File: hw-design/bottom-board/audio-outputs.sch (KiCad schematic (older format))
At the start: 54 parts, among them J10 NMJ6HCD2, J9 NMJ6HCD2, K1 G6S-2, K2 G6S-2, Q1 2N7002, Q2 2N7002, U11 OPA1678, U12 OPA1678

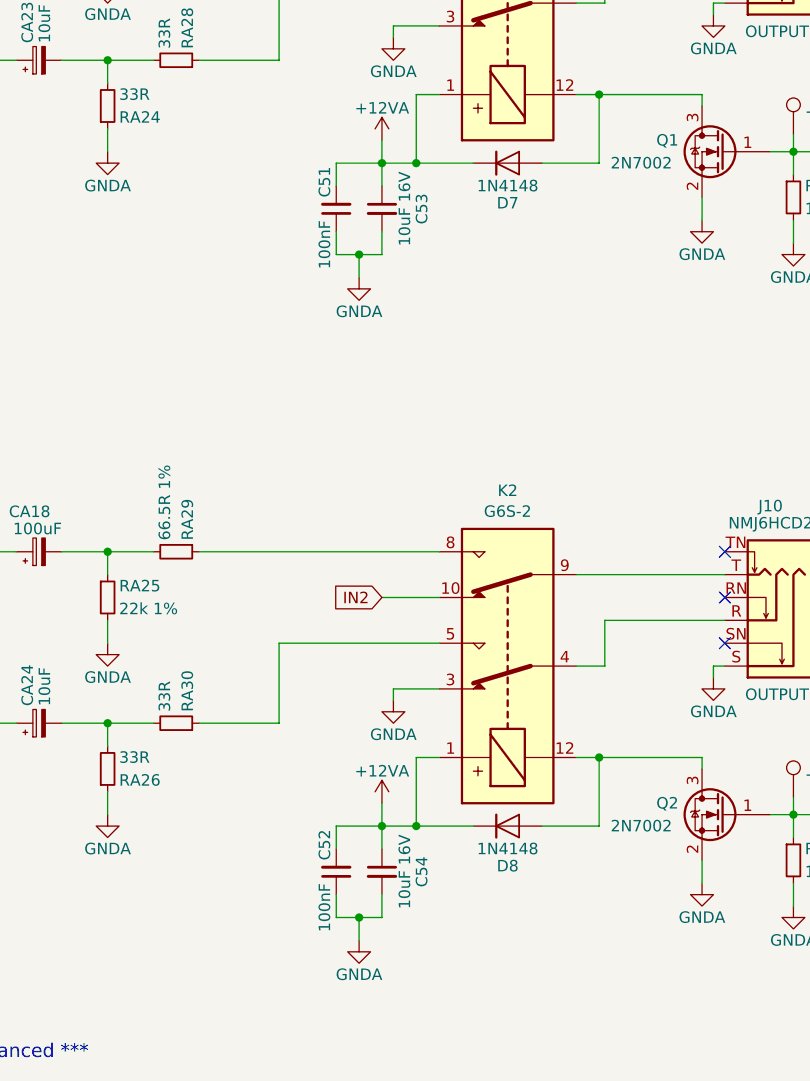
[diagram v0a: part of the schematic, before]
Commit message: increase filtering caps next to delay, less noise on low freqs
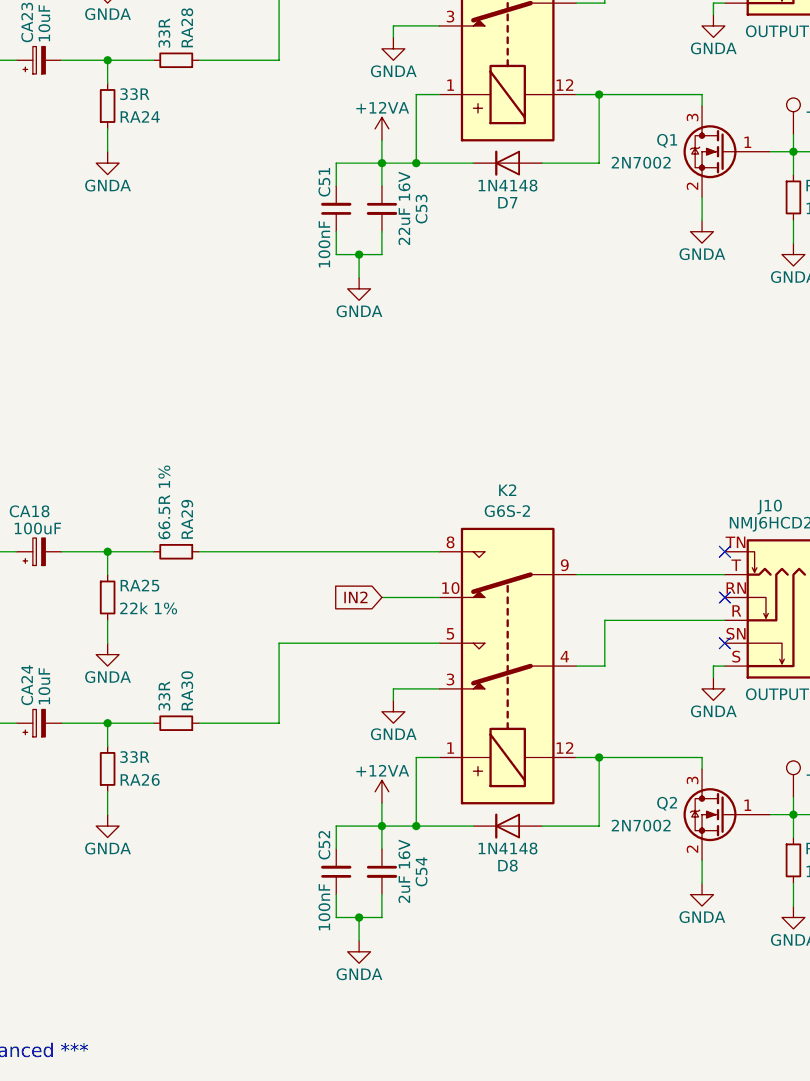
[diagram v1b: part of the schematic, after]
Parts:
- C53: value 10uF 16V -> 22uF 16V; MPN CL21A106KOFNNNE -> GRM21BC81C226ME44L; MPN2 C2012X5R1C106M085AC -> (none)
- C54: value 10uF 16V -> 2uF 16V; MPN CL21A106KOFNNNE -> GRM21BC81C226ME44L; MPN2 C2012X5R1C106M085AC -> (none)
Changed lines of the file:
@@
 AR Path="/54F72CD0/5BE997ED" Ref="C53"  Part="1"
 F 0 "C53" V 6625 3150 50  0000 C CNN
-F 1 "10uF 16V" V 6700 3150 50  0000 C CNN
+F 1 "22uF 16V" V 6700 3150 50  0000 C CNN
 F 2 "Capacitor_SMD:C_0805_2012Metric" H 6800 3150 60  0001 C CNN
 F 3 "" H 6800 3150 60  0000 C CNN
-F 4 "CL21A106KOFNNNE" H 1500 -2200 50  0001 C CNN "MPN"
-F 5 "C2012X5R1C106M085AC" H 6800 3150 50  0001 C CNN "MPN2"
+F 4 "GRM21BC81C226ME44L" H 1500 -2200 50  0001 C CNN "MPN"
 	1    6800 3150
 	-1   0    0    -1
@@
 AR Path="/54F72CD0/5BE9AFFC" Ref="C54"  Part="1"
 F 0 "C54" V 6625 6050 50  0000 C CNN
-F 1 "10uF 16V" V 6700 6050 50  0000 C CNN
+F 1 "2uF 16V" V 6700 6050 50  0000 C CNN
 F 2 "Capacitor_SMD:C_0805_2012Metric" H 6800 6050 60  0001 C CNN
 F 3 "" H 6800 6050 60  0000 C CNN
-F 4 "CL21A106KOFNNNE" H 1500 700 50  0001 C CNN "MPN"
-F 5 "C2012X5R1C106M085AC" H 6800 6050 50  0001 C CNN "MPN2"
+F 4 "GRM21BC81C226ME44L" H 1500 700 50  0001 C CNN "MPN"
 	1    6800 6050
 	-1   0    0    -1

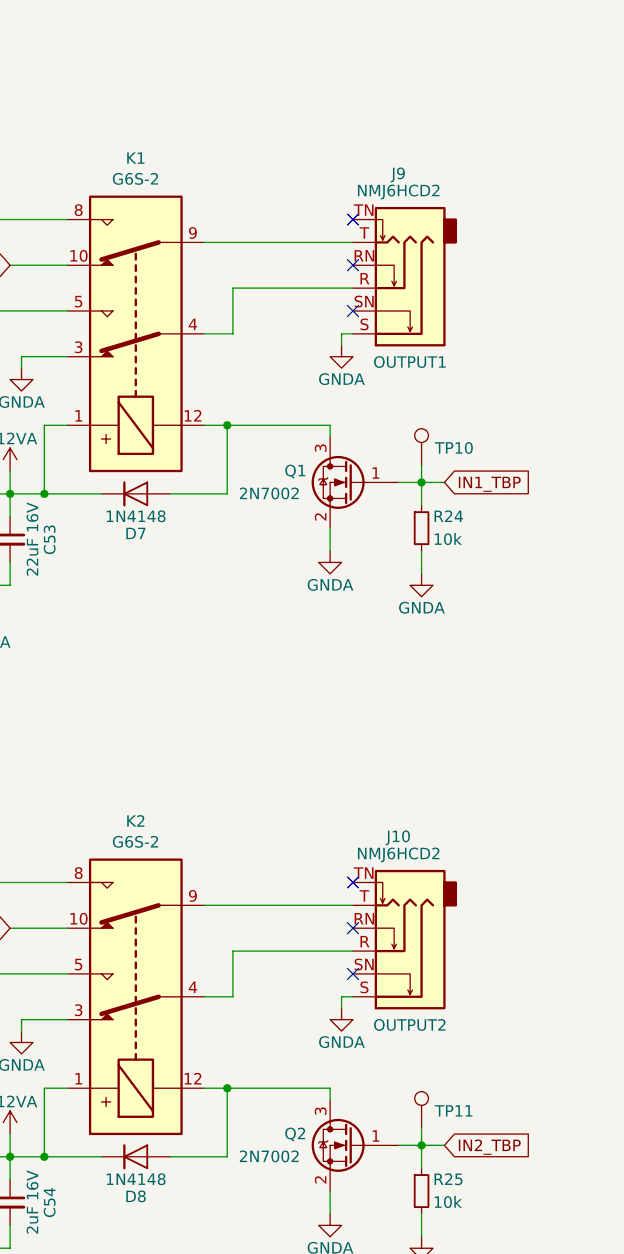
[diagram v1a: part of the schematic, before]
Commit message: added holes for new adapter + add jack detection
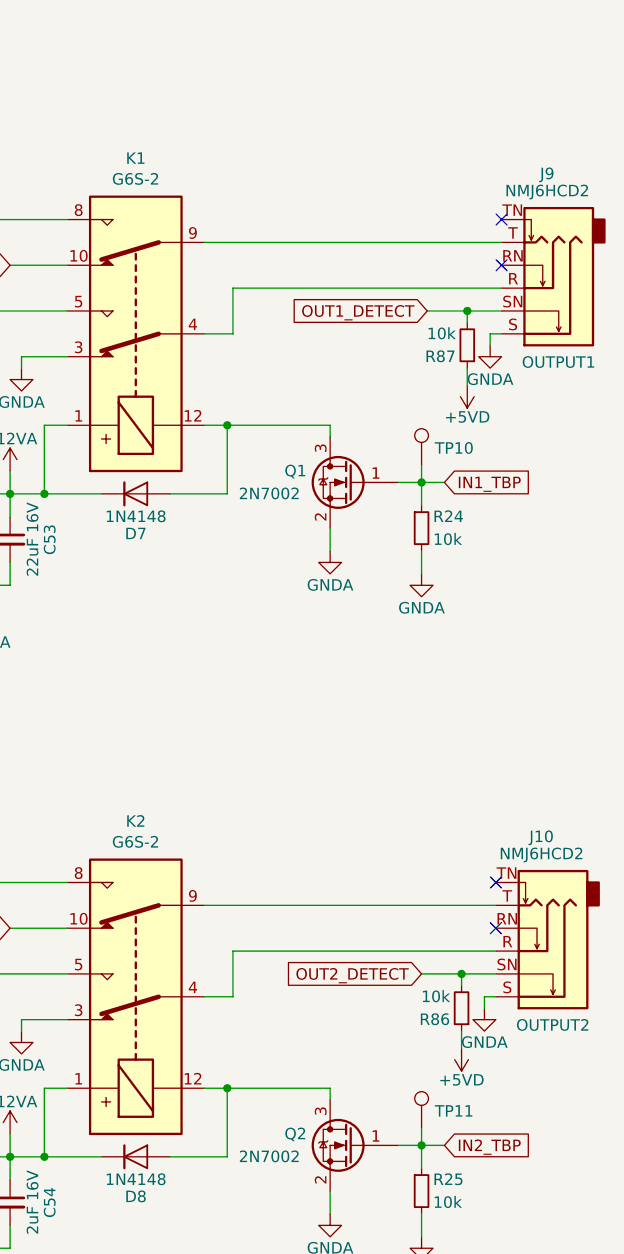
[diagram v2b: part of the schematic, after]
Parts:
- added R86, R87: 10k, Resistor_SMD:R_0603_1608Metric, symbol bottom-board-rescue:R_Small-Device
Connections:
- net OUT1_DETECT: now reaches J9.SN
- net OUT1_DETECT: now also R87.2
- net OUT2_DETECT: now reaches J10.SN
- net OUT2_DETECT: now also R86.2
- new net +5VD: R86.1, R87.1
- no-connect marks 6 -> 4
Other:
- moved on the sheet: J10, J9
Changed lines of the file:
@@
 L bottom-board-rescue:AudioJack3_Switch-Connector J9
 U 1 1 5B54B112
-P 8500 2050
-F 0 "J9" H 8500 1550 50  0000 C CNN
-F 1 "NMJ6HCD2" H 8500 1625 50  0000 C CNN
-F 2 "footprints:NMJ6HCD2" H 8750 2150 50  0001 C CNN
-F 3 "" H 8750 2150 50  0001 C CNN
-F 4 "NMJ6HCD2" H 8500 2050 60  0001 C CNN "MPN"
-F 5 "OUTPUT1" H 8450 2375 50  0000 C CNN "Comment"
-	1    8500 2050
+P 9150 2050
+F 0 "J9" H 9150 1550 50  0000 C CNN
+F 1 "NMJ6HCD2" H 9150 1625 50  0000 C CNN
+F 2 "footprints:NMJ6HCD2" H 9400 2150 50  0001 C CNN
+F 3 "" H 9400 2150 50  0001 C CNN
+F 4 "NMJ6HCD2" H 9150 2050 60  0001 C CNN "MPN"
+F 5 "OUTPUT1" H 9100 2375 50  0000 C CNN "Comment"
+	1    9150 2050
 	-1   0    0    1
 $EndComp
@@
 L bottom-board-rescue:GNDA-power #PWR0135
 U 1 1 5B54B119
-P 8250 2300
-F 0 "#PWR0135" H 8250 2050 50  0001 C CNN
-F 1 "GNDA" H 8250 2150 50  0000 C CNN
-F 2 "" H 8250 2300 60  0000 C CNN
-F 3 "" H 8250 2300 60  0000 C CNN
-	1    8250 2300
-	1    0    0    -1
-$EndComp
-NoConn ~ 8300 2150
-NoConn ~ 8300 1950
-NoConn ~ 8300 1750
+P 8900 2300
+F 0 "#PWR0135" H 8900 2050 50  0001 C CNN
+F 1 "GNDA" H 8900 2150 50  0000 C CNN
+F 2 "" H 8900 2300 60  0000 C CNN
+F 3 "" H 8900 2300 60  0000 C CNN
+	1    8900 2300
+	1    0    0    -1
+$EndComp
+NoConn ~ 8950 1950
+NoConn ~ 8950 1750
 Text GLabel 1950 4450 0    50   Input ~ 0
 CODEC_DAC_B
@@
 	6350 2500 6000 2500
 Wire Wire Line
-	8250 2300 8250 2250
+	8900 2300 8900 2250
 Wire Wire Line
 	5400 4650 5600 4650
@@
 $EndComp
 Wire Wire Line
-	8300 2250 8250 2250
-Wire Wire Line
-	7650 1850 8300 1850
-Wire Wire Line
-	8300 2050 7775 2050
+	8950 2250 8900 2250
 Wire Wire Line
 	7775 2050 7775 2250
@@
 L bottom-board-rescue:AudioJack3_Switch-Connector J10
 U 1 1 5B8682E0
-P 8500 4950
-F 0 "J10" H 8500 4450 50  0000 C CNN
-F 1 "NMJ6HCD2" H 8500 4525 50  0000 C CNN
-F 2 "footprints:NMJ6HCD2" H 8750 5050 50  0001 C CNN
-F 3 "" H 8750 5050 50  0001 C CNN
-F 4 "NMJ6HCD2" H 8500 4950 60  0001 C CNN "MPN"
-F 5 "OUTPUT2" H 8450 5275 50  0000 C CNN "Comment"
-	1    8500 4950
+P 9125 4950
+F 0 "J10" H 9125 4450 50  0000 C CNN
+F 1 "NMJ6HCD2" H 9125 4525 50  0000 C CNN
+F 2 "footprints:NMJ6HCD2" H 9375 5050 50  0001 C CNN
+F 3 "" H 9375 5050 50  0001 C CNN
+F 4 "NMJ6HCD2" H 9125 4950 60  0001 C CNN "MPN"
+F 5 "OUTPUT2" H 9075 5275 50  0000 C CNN "Comment"
+	1    9125 4950
 	-1   0    0    1
 $EndComp
@@
 L bottom-board-rescue:GNDA-power #PWR0136
 U 1 1 5B8682E6
-P 8250 5200
-F 0 "#PWR0136" H 8250 4950 50  0001 C CNN
-F 1 "GNDA" H 8250 5050 50  0000 C CNN
-F 2 "" H 8250 5200 60  0000 C CNN
-F 3 "" H 8250 5200 60  0000 C CNN
-	1    8250 5200
-	1    0    0    -1
-$EndComp
-NoConn ~ 8300 5050
-NoConn ~ 8300 4850
-NoConn ~ 8300 4650
-Wire Wire Line
-	8250 5200 8250 5150
-Wire Wire Line
-	8300 5150 8250 5150
-Wire Wire Line
-	7650 4750 8300 4750
-Wire Wire Line
-	8300 4950 7775 4950
+P 8875 5200
+F 0 "#PWR0136" H 8875 4950 50  0001 C CNN
+F 1 "GNDA" H 8875 5050 50  0000 C CNN
+F 2 "" H 8875 5200 60  0000 C CNN
+F 3 "" H 8875 5200 60  0000 C CNN
+	1    8875 5200
+	1    0    0    -1
+$EndComp
+NoConn ~ 8925 4850
+NoConn ~ 8925 4650
+Wire Wire Line
+	8875 5200 8875 5150
+Wire Wire Line
+	8925 5150 8875 5150
 Wire Wire Line
 	7775 4950 7775 5150
@@
 Wire Wire Line
 	850  6600 925  6600
+$Comp
+L bottom-board-rescue:R_Small-Device R?
+U 1 1 5DF9BAE3
+P 8800 2300
+AR Path="/5B3B40FB/5DF9BAE3" Ref="R?"  Part="1"
+AR Path="/54F72C8D/5DF9BAE3" Ref="R?"  Part="1"
+AR Path="/54F72CD0/5DF9BAE3" Ref="R87"  Part="1"
+F 0 "R87" H 8850 2350 50  0000 L CNN
+F 1 "10k" H 8850 2250 50  0000 L CNN
+F 2 "Resistor_SMD:R_0603_1608Metric" H 8800 2300 60  0001 C CNN
+F 3 "" H 8800 2300 60  0000 C CNN
+F 4 "RMCF0603JT10K0" H 2050 -675 50  0001 C CNN "MPN"
+F 5 "RCA060310K0JNEA" H 2050 -675 50  0001 C CNN "MPN2"
+F 6 "ESR03EZPJ103" H 2050 -675 50  0001 C CNN "MPN3"
+	1    8800 2300
+	-1   0    0    1
+$EndComp
+Text GLabel 8625 2150 0    50   Input ~ 0
+OUT1_DETECT
+Wire Wire Line
+	8625 2150 8800 2150
+Wire Wire Line
+	8800 2200 8800 2150
+Connection ~ 8800 2150
+Wire Wire Line
+	8800 2150 8950 2150
+Wire Wire Line
+	8800 2400 8800 2475
+Wire Wire Line
+	7650 1850 8950 1850
+Wire Wire Line
+	7775 2050 8950 2050
+Wire Wire Line
+	7650 4750 8925 4750
+Wire Wire Line
+	7775 4950 8925 4950
+$Comp
+L bottom-board-rescue:R_Small-Device R?
+U 1 1 5E033F13
+P 8775 5200
+AR Path="/5B3B40FB/5E033F13" Ref="R?"  Part="1"
+AR Path="/54F72C8D/5E033F13" Ref="R?"  Part="1"
+AR Path="/54F72CD0/5E033F13" Ref="R86"  Part="1"
+F 0 "R86" H 8825 5250 50  0000 L CNN
+F 1 "10k" H 8825 5150 50  0000 L CNN
+F 2 "Resistor_SMD:R_0603_1608Metric" H 8775 5200 60  0001 C CNN
+F 3 "" H 8775 5200 60  0000 C CNN
+F 4 "RMCF0603JT10K0" H 2025 2225 50  0001 C CNN "MPN"
+F 5 "RCA060310K0JNEA" H 2025 2225 50  0001 C CNN "MPN2"
+F 6 "ESR03EZPJ103" H 2025 2225 50  0001 C CNN "MPN3"
+	1    8775 5200
+	-1   0    0    1
+$EndComp
+Text GLabel 8600 5050 0    50   Input ~ 0
+OUT2_DETECT
+Wire Wire Line
+	8600 5050 8775 5050
+Wire Wire Line
+	8775 5100 8775 5050
+Connection ~ 8775 5050
+Wire Wire Line
+	8775 5050 8925 5050
+Wire Wire Line
+	8775 5300 8775 5375
+$Comp
+L bottom-board-rescue:+5VD-power #PWR?
+U 1 1 5E152686
+P 8775 5375
+F 0 "#PWR?" H 8775 5225 50  0001 C CNN
+F 1 "+5VD" H 8775 5515 50  0000 C CNN
+F 2 "" H 8775 5375 50  0001 C CNN
+F 3 "" H 8775 5375 50  0001 C CNN
+	1    8775 5375
+	-1   0    0    1
+$EndComp
+$Comp
+L bottom-board-rescue:+5VD-power #PWR?
+U 1 1 5E1625ED
+P 8800 2475
+F 0 "#PWR?" H 8800 2325 50  0001 C CNN
+F 1 "+5VD" H 8800 2615 50  0000 C CNN
+F 2 "" H 8800 2475 50  0001 C CNN
+F 3 "" H 8800 2475 50  0001 C CNN
+	1    8800 2475
+	-1   0    0    1
+$EndComp
 $EndSCHEMATC

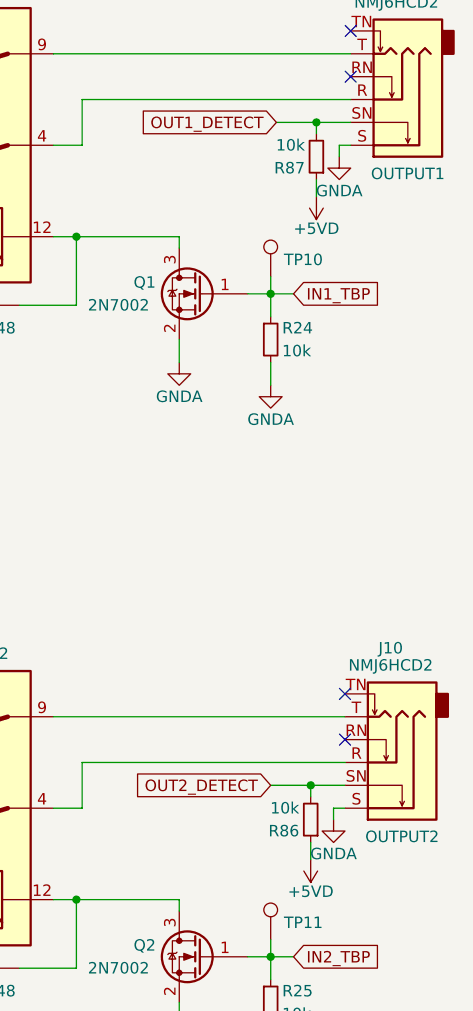
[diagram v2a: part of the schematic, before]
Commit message: move DC filter + add fabrication files
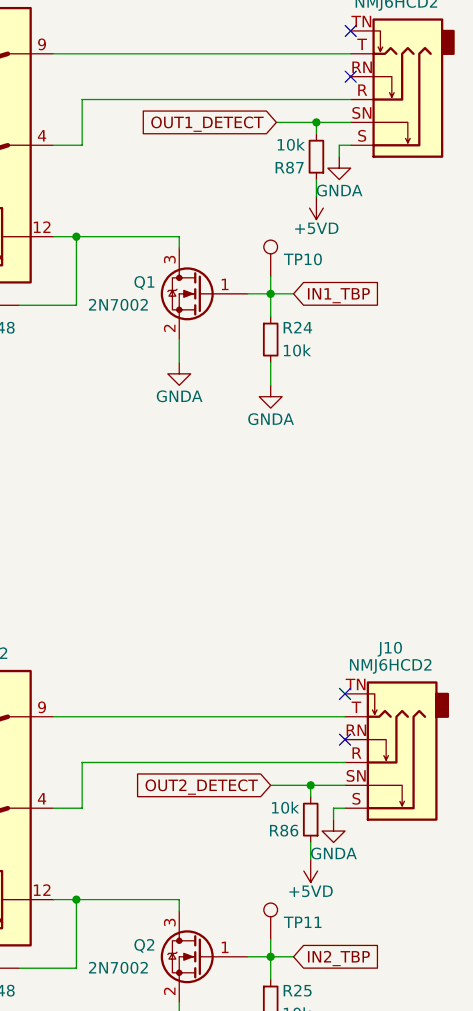
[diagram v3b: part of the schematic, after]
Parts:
- C11, C13, C38: MPN2 C2012X5R1C106M085AC -> (none)
- C12, C14, C51, C52: MPN2 C0603X104K8RACTU -> (none); MPN3 CS0603KRX7R7BB104 -> (none)
- CA11, CA12, CA23, CA24: MPN2 UWT1C100MCL1GB -> (none); MPN3 EDH106M016A9BAA -> (none)
- CA13, CA14, CA15, CA16: MPN2 06035A101FAT2A -> (none); MPN3 CC0603JRNPO8BN101 -> (none)
- CA17, CA18: MPN2 EEE-HA1C101WP -> (none); MPN3 EEV107M016A9GAA -> (none)
- D7, D8: MPN2 1N4148WS-7-F -> (none); MPN3 1N4148WS-G RVG -> (none)
- J10: Comment OUTPUT2 -> (none); MPN NMJ6HCD2 -> NYS215
- J9: Comment OUTPUT1 -> (none); MPN NMJ6HCD2 -> NYS215
- K1, K2: MPN2 G6S-2F-TR DC12 -> (none)
- Q1, Q2: MPN2 2N7002K-7 -> (none); MPN3 TSM2N7002KCX RFG -> (none)
- R24, R25, R86, R87: MPN2 RCA060310K0JNEA -> (none); MPN3 ESR03EZPJ103 -> (none)
- RA15, RA16, RA17, RA18, RA19, RA20, RA21, RA22, RA43, RA44, RA45, RA46: MPN2 RT0603DRE0710KL -> (none); MPN3 ERJ-PB3D1002V -> (none)
- RA23, RA25: MPN2 RT0603DRE0722KL -> (none); MPN3 ERJ-PB3D2202V -> (none)
- RA24, RA26, RA28, RA30: MPN2 RR0816Q-330-D -> (none); MPN3 RNCF0603DTC33R2 -> (none)
- RA27, RA29: MPN2 RT0603DRE0766R5L -> (none); MPN3 RNCF0603DTC66R5 -> (none)

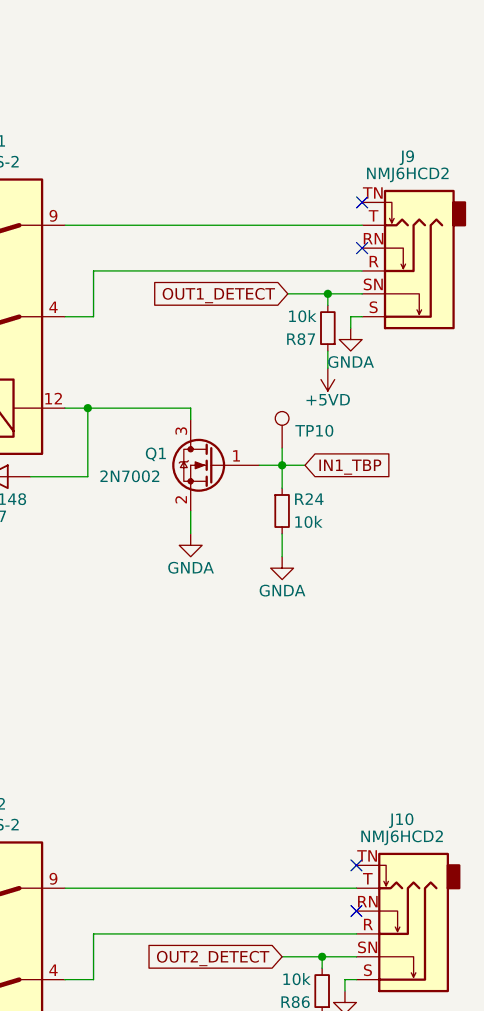
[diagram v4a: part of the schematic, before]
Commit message: update jack + dc barrel connector MPN
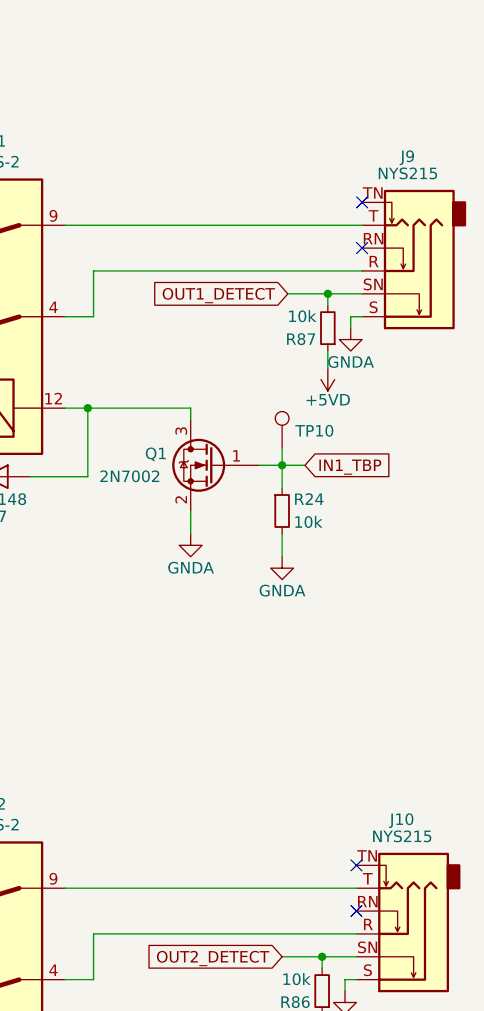
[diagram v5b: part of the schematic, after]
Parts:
- J10, J9: value NMJ6HCD2 -> NYS215
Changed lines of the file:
@@
 P 9150 2050
 F 0 "J9" H 9150 1550 50  0000 C CNN
-F 1 "NMJ6HCD2" H 9150 1625 50  0000 C CNN
+F 1 "NYS215" H 9150 1625 50  0000 C CNN
 F 2 "footprints:NMJ6HCD2" H 9400 2150 50  0001 C CNN
 F 3 "" H 9400 2150 50  0001 C CNN
@@
 P 9125 4950
 F 0 "J10" H 9125 4450 50  0000 C CNN
-F 1 "NMJ6HCD2" H 9125 4525 50  0000 C CNN
+F 1 "NYS215" H 9125 4525 50  0000 C CNN
 F 2 "footprints:NMJ6HCD2" H 9375 5050 50  0001 C CNN
 F 3 "" H 9375 5050 50  0001 C CNN
